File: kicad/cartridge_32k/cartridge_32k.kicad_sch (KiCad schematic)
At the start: 7 parts, among them J1 Card edge (87715-9106 mate), U1 ATF22V10C-7PX, U2 AT28C256-15PU, U3 AS7C256C-15PCN

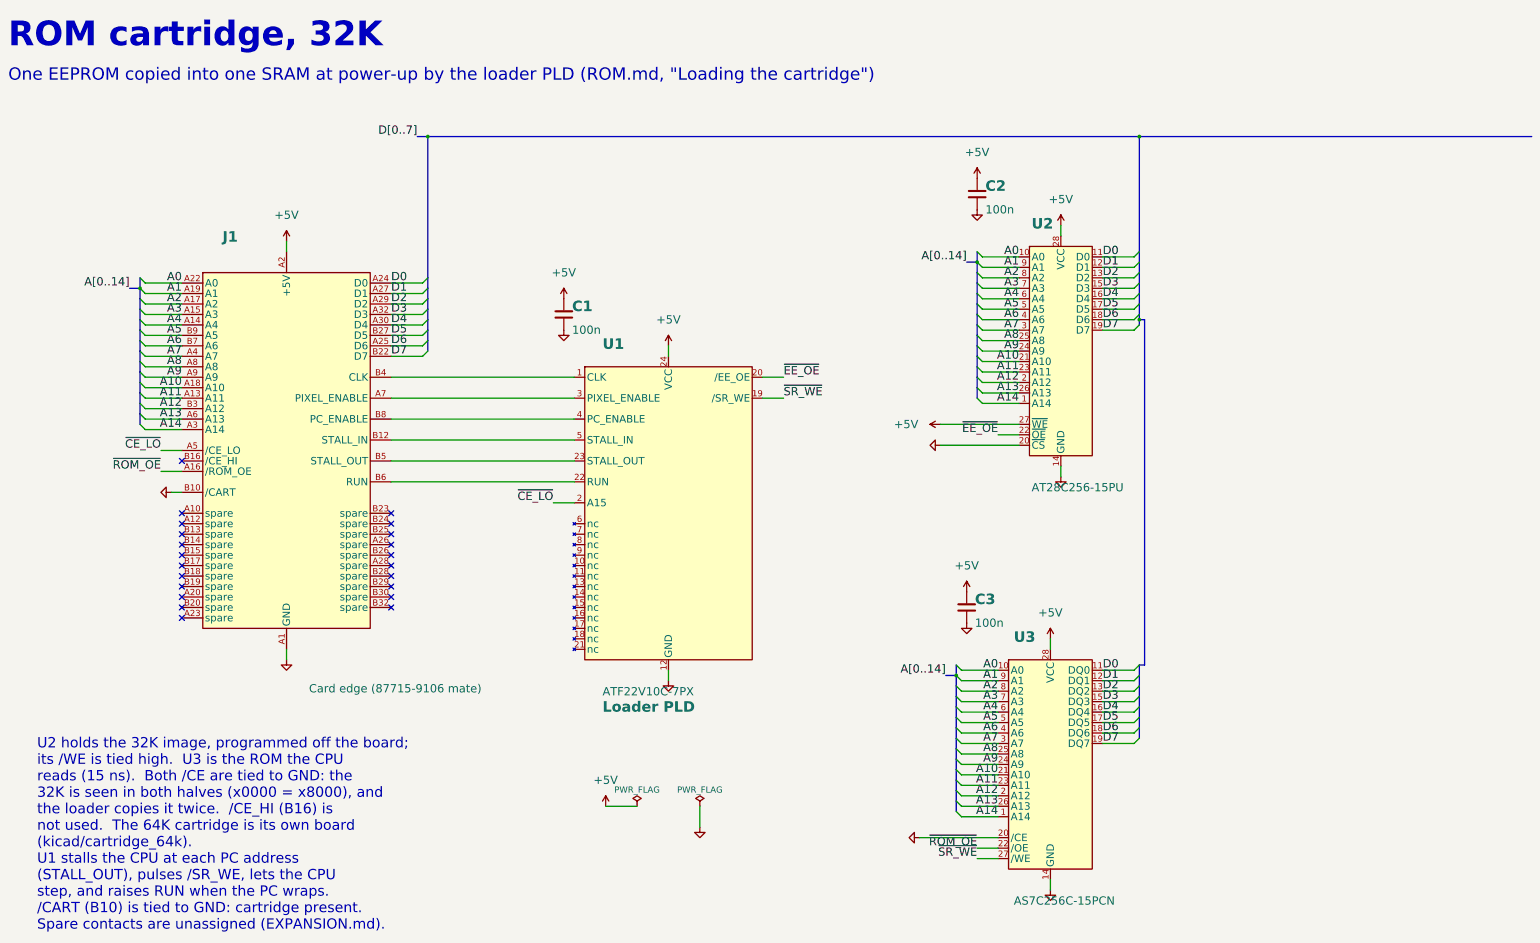
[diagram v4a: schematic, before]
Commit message: Schematic: rename buses to ADDR / DATABUS / D, wire the shared port outputs
- Address bus A15:A0 is now ADDR15:ADDR0, the data bus D7:D0 is DATABUS7:DATABUS0
  and the D register's outputs DR7:DR0 are D7:D0 (main board and both cartridges).
- Shared port sheet: U38's outputs P_SCK, P_MOSI, P_CS, P_PS2D and K0 are wired
  to the SNES pads, the SD dividers and the PS/2 hold diodes (K0 -> D6 ->
  keyboard CLK).  J3 now sits level with U38's SCK/MOSI pins, J2 above it.
- Parts moved so the longer labels fit: U3/U4 and the PC bus, U18, U22, U11,
  U31, U32, RN1, R5-R12; expansion slots in two rows.
- SCHEMATIC_PLAN.md: the bus names.

Co-Authored-By: Claude Opus 5.5 <noreply@anthropic.com>
Claude-Session: https://claude.ai/code/session_01DnW5SUv7E4nz9tGtPvD1qV
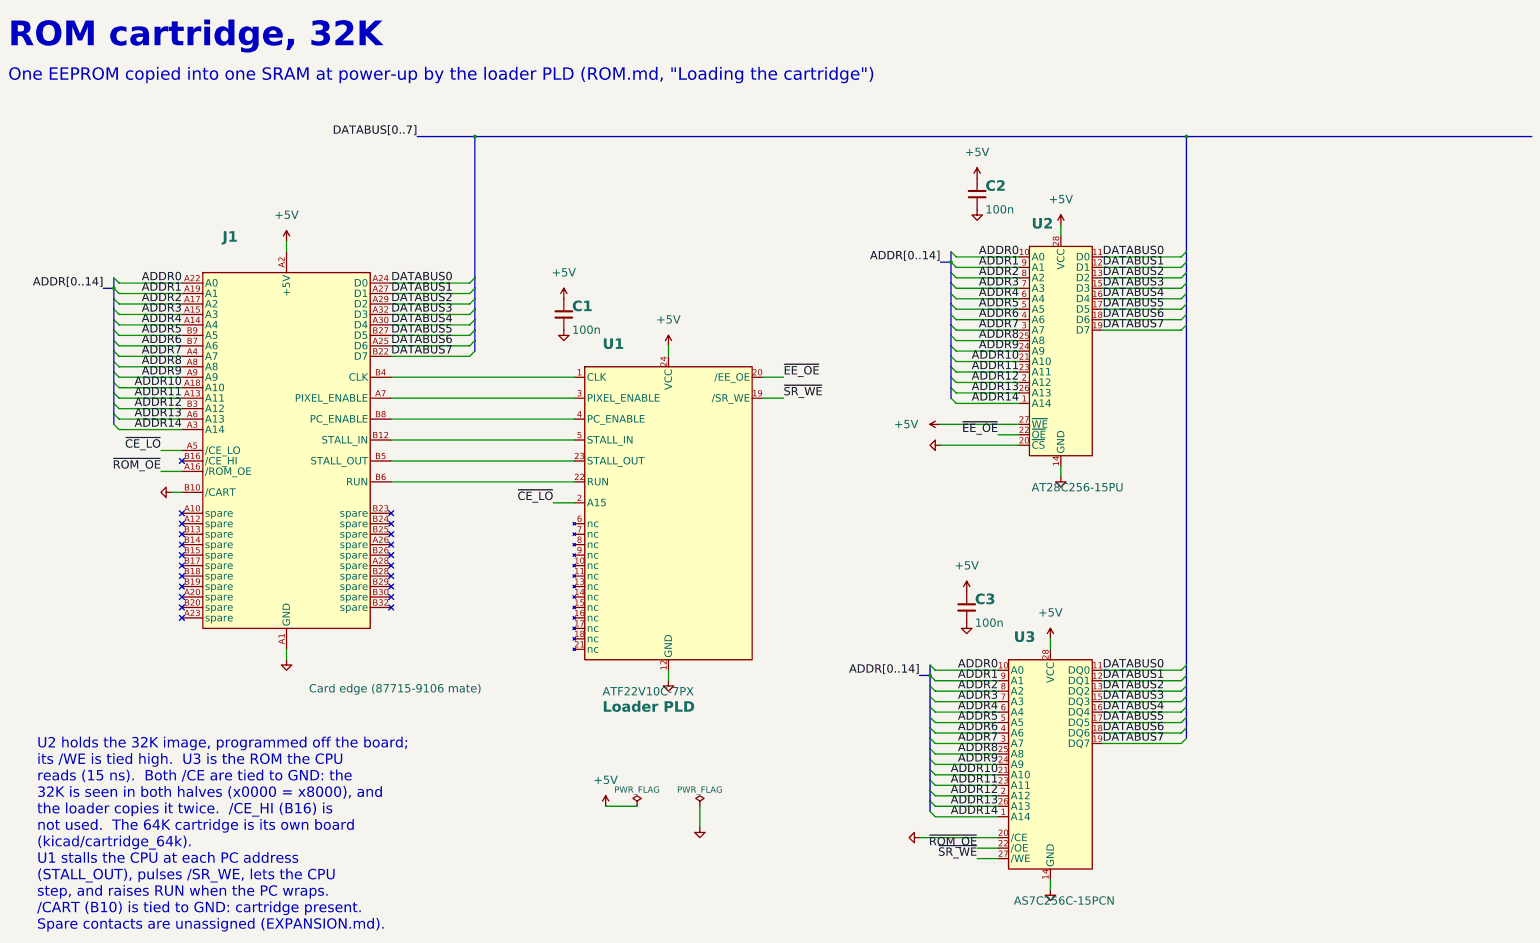
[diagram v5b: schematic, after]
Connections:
- net A0 renamed ADDR0
- net A1 renamed ADDR1
- net A10 renamed ADDR10
- net A11 renamed ADDR11
- net A12 renamed ADDR12
- net A13 renamed ADDR13
- net A14 renamed ADDR14
- net A2 renamed ADDR2
- net A3 renamed ADDR3
- net A4 renamed ADDR4
- net A5 renamed ADDR5
- net A6 renamed ADDR6
- net A7 renamed ADDR7
- net A8 renamed ADDR8
- net A9 renamed ADDR9
- net D0 renamed DATABUS0
- net D1 renamed DATABUS1
- net D2 renamed DATABUS2
- net D3 renamed DATABUS3
- net D4 renamed DATABUS4
- net D5 renamed DATABUS5
- net D6 renamed DATABUS6
- net D7 renamed DATABUS7
